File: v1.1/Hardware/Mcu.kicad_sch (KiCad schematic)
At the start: 17 parts, among them J2 Conn_02x08_Counter_Clockwise, J5 Conn_01x04, U15 STM32F103CBTx, Y1 8MHz

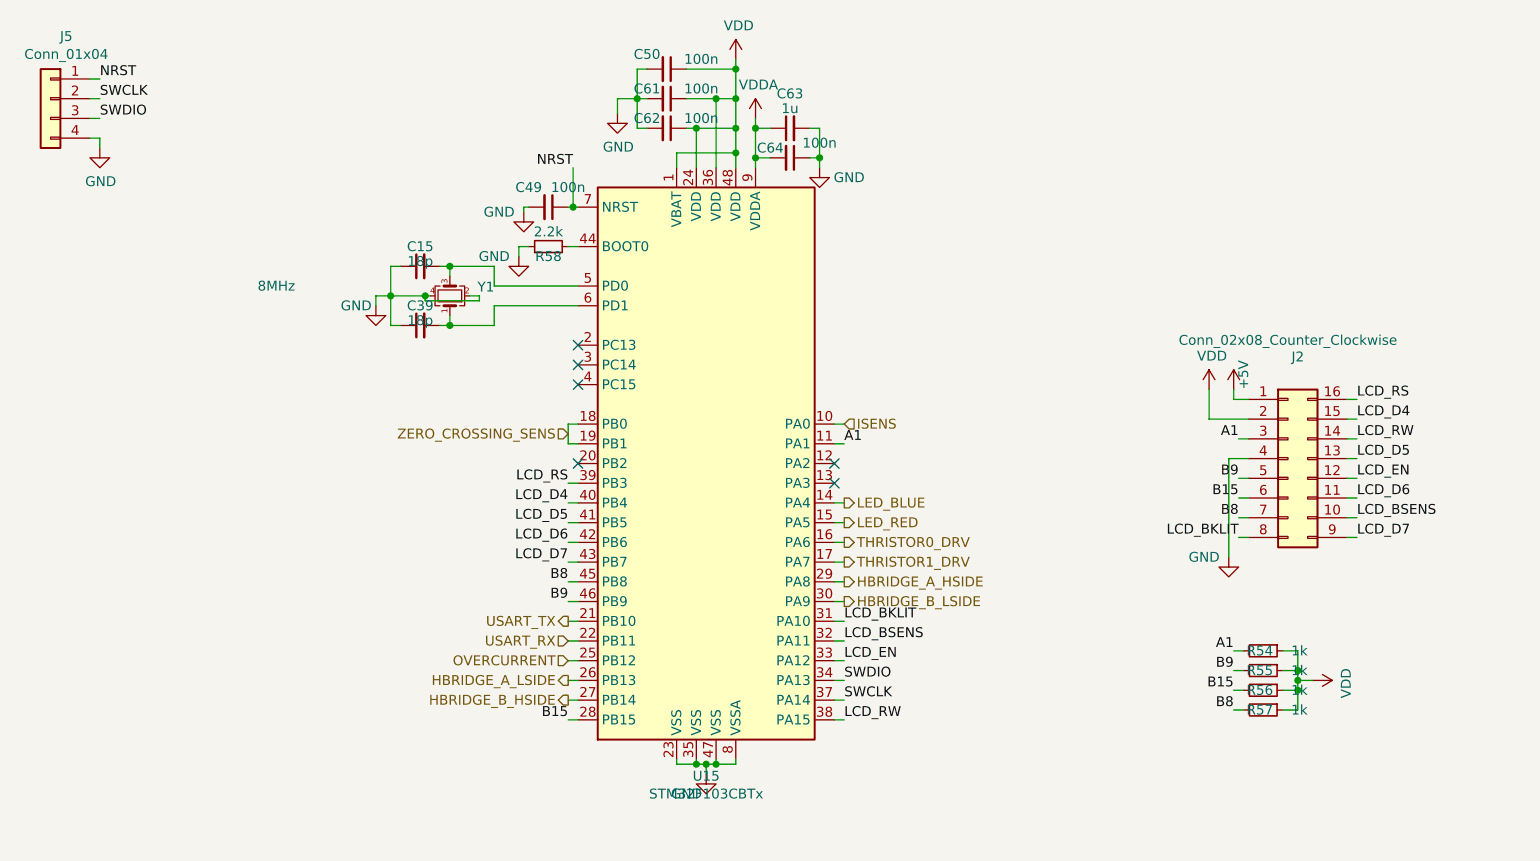
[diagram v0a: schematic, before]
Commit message: v1.1&v1.2 PCB addition.
#####v1.1#####
+Change of MCU; STM32F334C8T6 instead of STM32F103C8T6.
+Filtering 3rd order components of the square wave.
+Use  4 capacitors.
+Adapted to generic transformer(primary 6.4mH, secondary 14.4mH)
+Faster IGBT.

########v1.2#######
+Measures only PZT current and voltage.
+Differential inputs.
+Analog circuitry is capable of measuring four quadrant voltage, current and complex impedance.
+Half bridge configuration.
+Gate resistance of the IGBT's lowered.
+Only USART based touch panel can be connected; not conventional LCD.
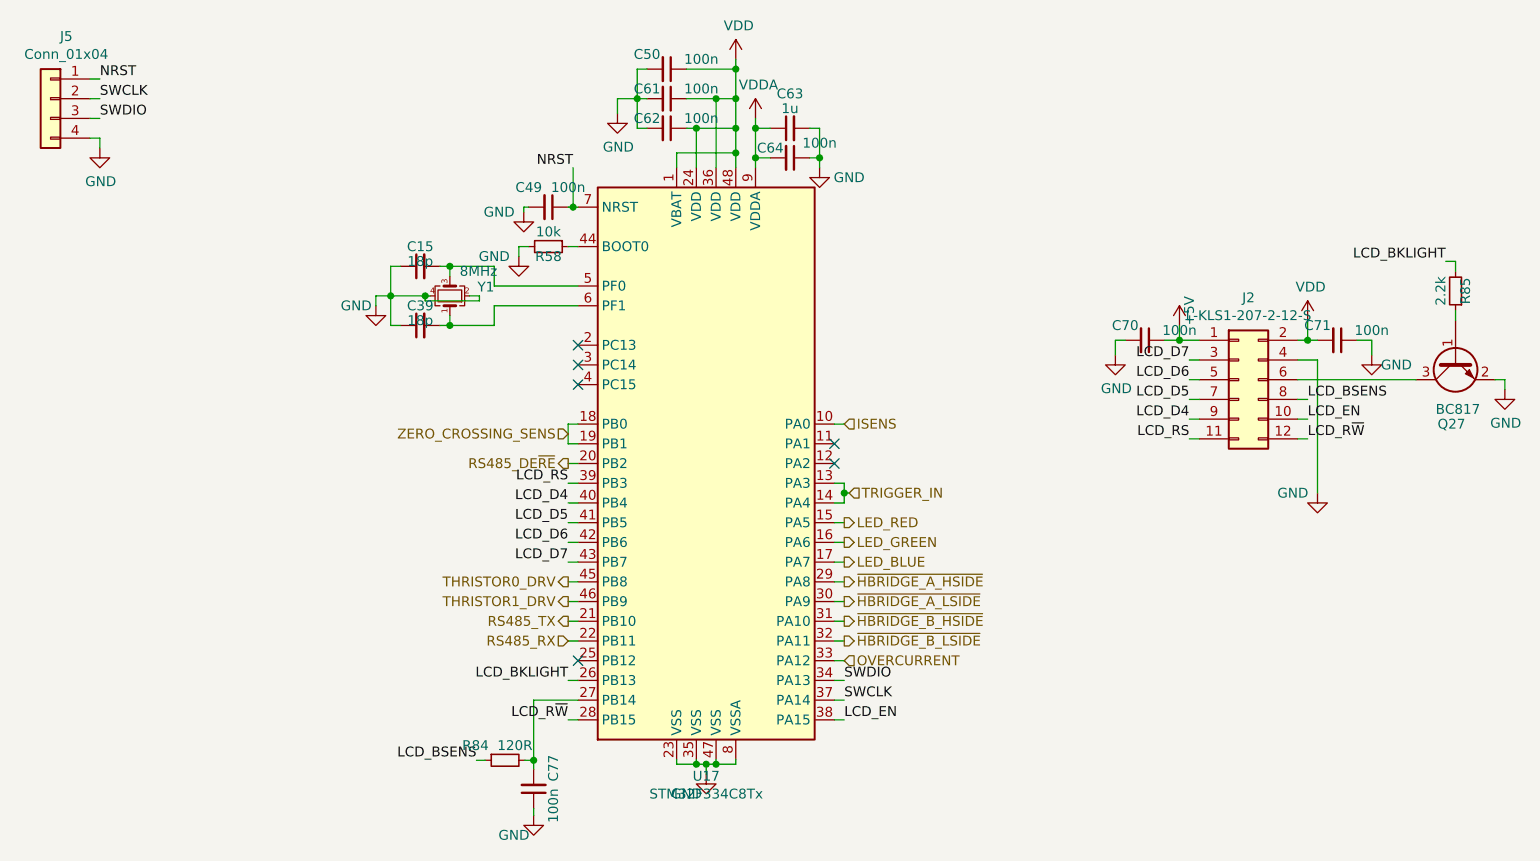
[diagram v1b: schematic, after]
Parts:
- removed J2: Conn_02x08_Counter_Clockwise, Connector_PinHeader_2.54mm:PinHeader_2x08_P2.54mm_Vertical, symbol Connector_Generic:Conn_02x08_Counter_Clockwise
- removed R54, R55, R56, R57: 1k, Resistor_SMD:R_0805_2012Metric_Pad1.15x1.40mm_HandSolder, symbol Device:R_Small
- removed U15: STM32F103CBTx, Package_QFP:LQFP-48_7x7mm_P0.5mm, symbol MCU_ST_STM32F1:STM32F103CBTx
- added C70, C71, C77: 100n, Capacitor_SMD:C_0805_2012Metric, symbol Device:C_Small
- added J2: L-KLS1-207-2-12-S, Connector_PinHeader_2.54mm:PinHeader_2x06_P2.54mm_Vertical, symbol Connector_Generic:Conn_02x06_Odd_Even
- added Q27: BC817, Package_TO_SOT_SMD:SOT-23, symbol Transistor_BJT:BC817
- added R84: 120R, Resistor_SMD:R_0805_2012Metric, symbol Device:R_Small
- added R85: 2.2k, Resistor_SMD:R_0805_2012Metric, symbol Device:R_Small
- added U17: STM32F334C8Tx, Package_QFP:LQFP-48_7x7mm_P0.5mm, symbol MCU_ST_STM32F3:STM32F334C8Tx
- C15, C39: footprint Capacitor_SMD:C_0603_1608Metric_Pad1.05x0.95mm_HandSolder -> Capacitor_SMD:C_0603_1608Metric
- C49, C50, C61, C62, C63, C64: footprint Capacitor_SMD:C_0805_2012Metric_Pad1.15x1.40mm_HandSolder -> Capacitor_SMD:C_0805_2012Metric
- R58: value 2.2k -> 10k; footprint Resistor_SMD:R_0805_2012Metric_Pad1.15x1.40mm_HandSolder -> Resistor_SMD:R_0805_2012Metric; Link https://ozdisan.com/passive-components/resistors/smt-smd-and-chip-resistors/0805S8J0222T5E -> https://ozdisan.com/passive-components/resistors/smt-smd-and-chip-resistors/0805S8J0103T5E; Price 0.01504TL -> 0.01518TL
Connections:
- net +5V: now also C70.1, J2.1 (Pin_1)
- net GND: now also R58.2, C70.2, C71.1, C77.1, J2.4 (Pin_4), Q27.2 (E), U17.23 (VSS), U17.35 (VSS), U17.47 (VSS), U17.8 (VSSA); no longer R58.1
- net ISENS: now also U17.10 (PA0)
- net LCD_BSENS: now also J2.8 (Pin_8), R84.1
- net LCD_D4: now also J2.9 (Pin_9), U17.40 (PB4)
- net LCD_D5: now also J2.7 (Pin_7), U17.41 (PB5)
- net LCD_D6: now also J2.5 (Pin_5), U17.42 (PB6)
- net LCD_D7: now also J2.3 (Pin_3), U17.43 (PB7)
- net LCD_EN: now also J2.10 (Pin_10), U17.38 (PA15)
- net LCD_RS: now also J2.11 (Pin_11), U17.39 (PB3)
- net LED_BLUE: now also U17.17 (PA7)
- net LED_RED: now also U17.15 (PA5)
- net NRST: now also U17.7 (NRST)
- net OVERCURRENT: now also U17.33 (PA12)
- net SWCLK: now also U17.37 (PA14)
- net SWDIO: now also U17.34 (PA13)
- net THRISTOR0_DRV: now also U17.45 (PB8)
- net THRISTOR1_DRV: now also U17.46 (PB9)
- net VDD: now also C71.2, J2.2 (Pin_2), U17.1 (VBAT), U17.24 (VDD), U17.36 (VDD), U17.48 (VDD)
- net VDDA: now also U17.9 (VDDA)
- net ZERO_CROSSING_SENS: now also U17.18 (PB0), U17.19 (PB1)
- net at C15.2, Y1.3: now also U17.5 (PF0)
- net at C39.2, Y1.1: now also U17.6 (PF1)
- new net: C77.2, R84.2, U17.27 (PB14)
- new net: R58.1, U17.44 (BOOT0)
- new net: Q27.1 (B), R85.1
- new net: J2.6 (Pin_6), Q27.3 (C)
- new net LCD_BKLIGHT: R85.2, U17.26 (PB13)
- new net LCD_R~W: J2.12 (Pin_12), U17.28 (PB15)
- new net LED_GREEN: U17.16 (PA6)
- new net RS485_DE~RE: U17.20 (PB2)
- new net RS485_RX: U17.22 (PB11)
- new net RS485_TX: U17.21 (PB10)
- new net TRIGGER_IN: U17.13 (PA3), U17.14 (PA4)
- new net ~HBRIDGE_A_HSIDE: U17.29 (PA8)
- new net ~HBRIDGE_A_LSIDE: U17.30 (PA9)
- new net ~HBRIDGE_B_HSIDE: U17.31 (PA10)
- new net ~HBRIDGE_B_LSIDE: U17.32 (PA11)
